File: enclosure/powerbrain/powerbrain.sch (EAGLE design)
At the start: 41 parts, among them J3 AVR_SPI_PRG_6PTH, Q1 FDD4141TO252, Q2 200mA/50V, U2 TPS61090, X2 ZX62D-B-5PA8

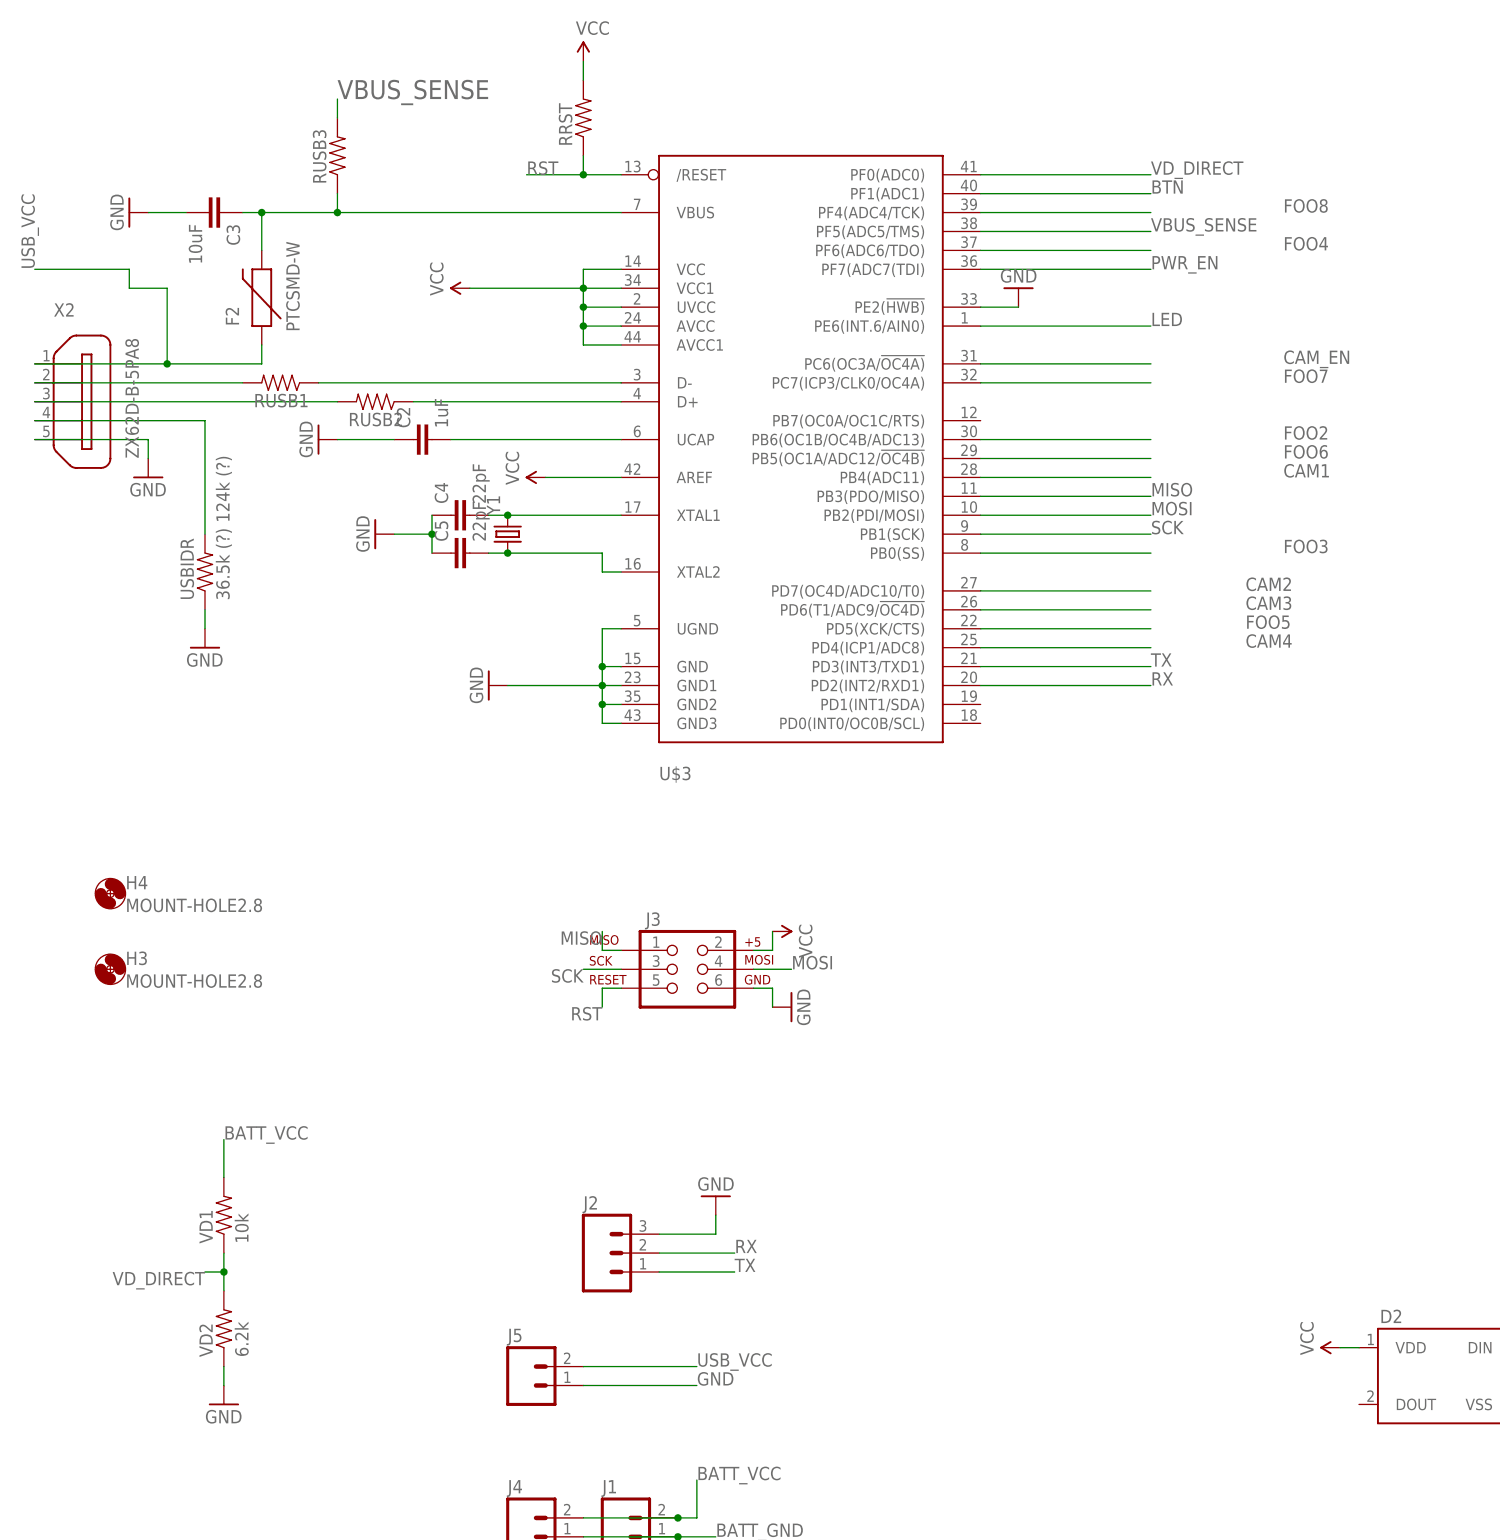
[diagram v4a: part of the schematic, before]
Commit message: powerbrain: VBUS switch
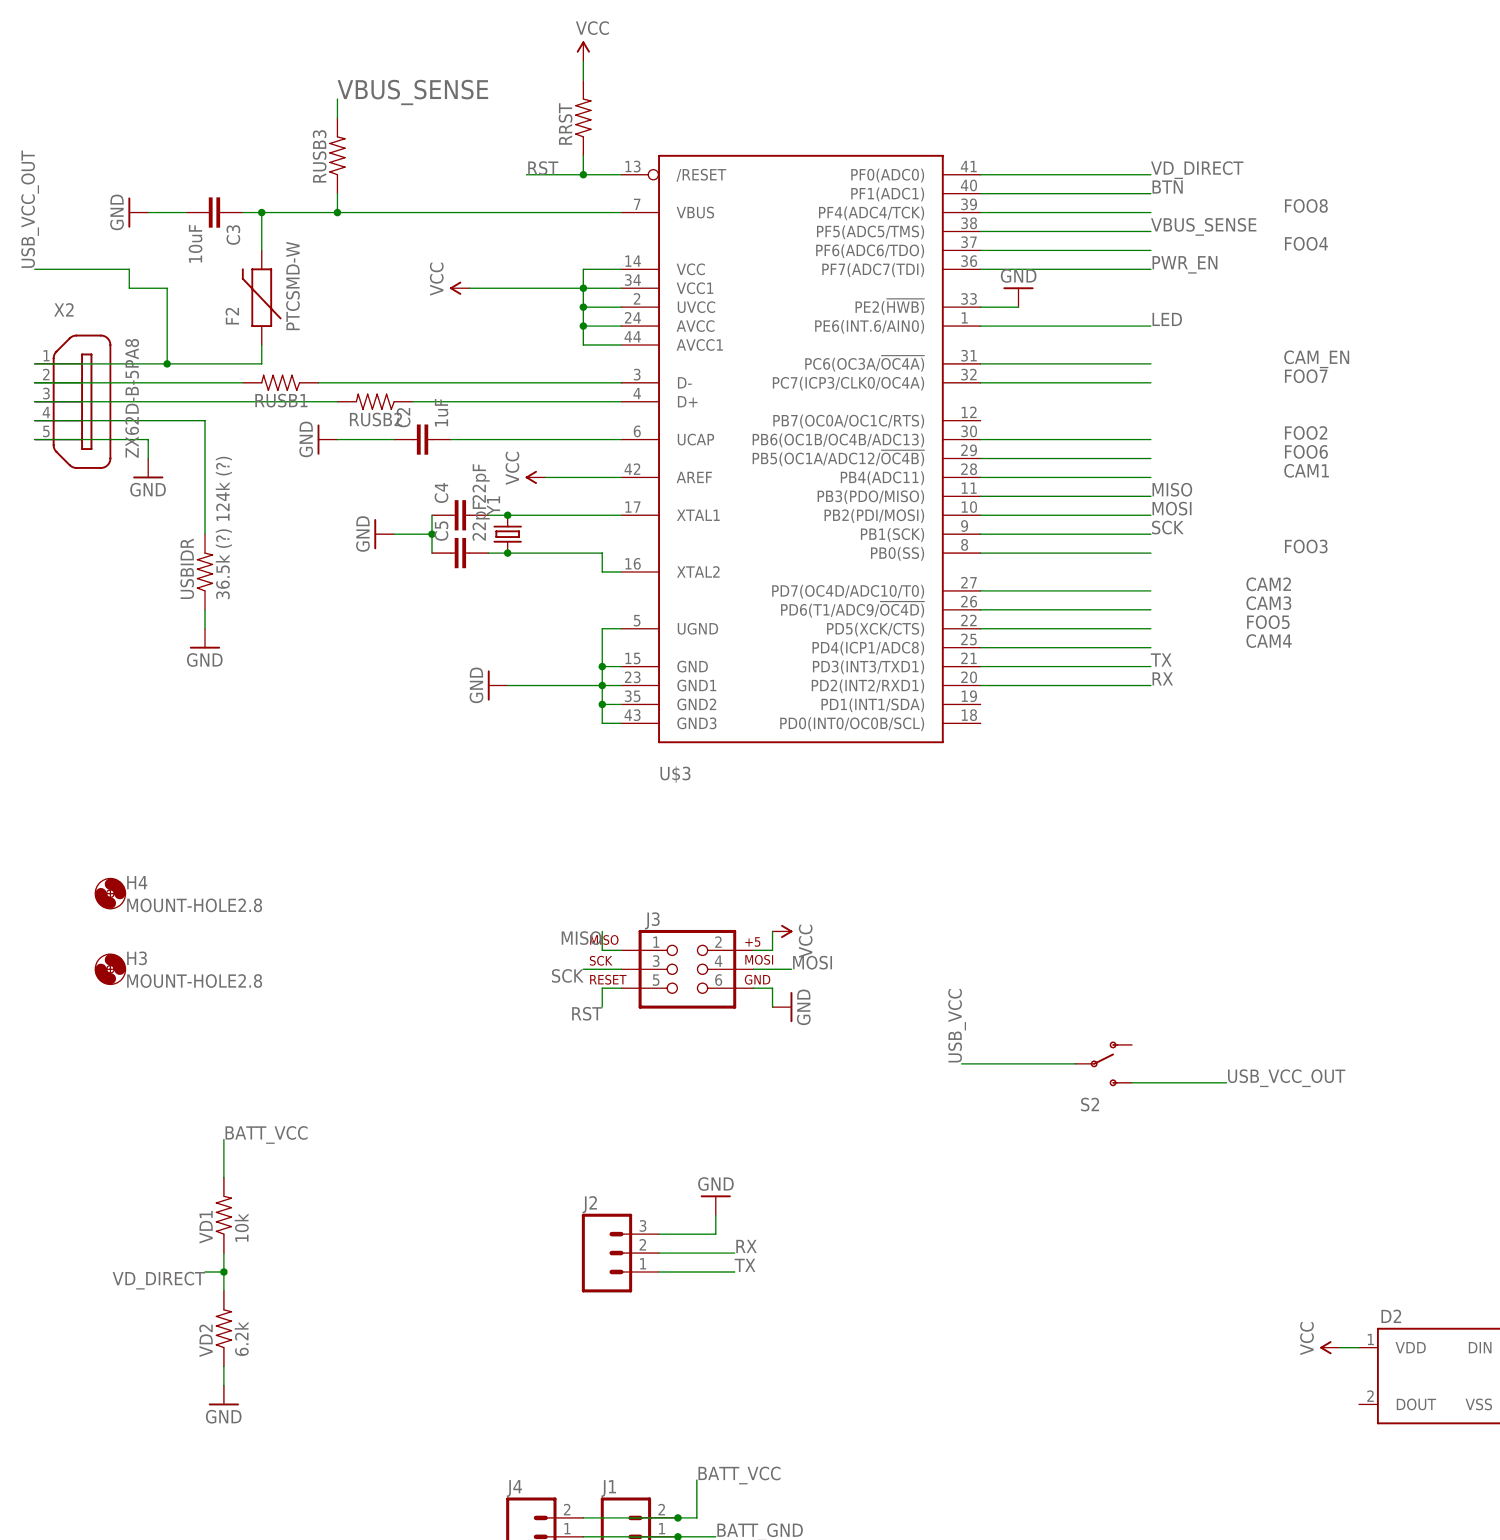
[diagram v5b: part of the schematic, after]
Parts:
- removed J5: (no value), SparkFun-Connectors:M02LOCK
- added S2: (no value), SparkFun-Electromechanical:SWITCH-SPDTSMD2
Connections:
- new net USB_VCC_OUT: F2.1, S2.S, X2G$1.1
- net GND: no longer J5.1
- net USB_VCC: now also S2.P; no longer F2.1, J5.2, X2G$1.1

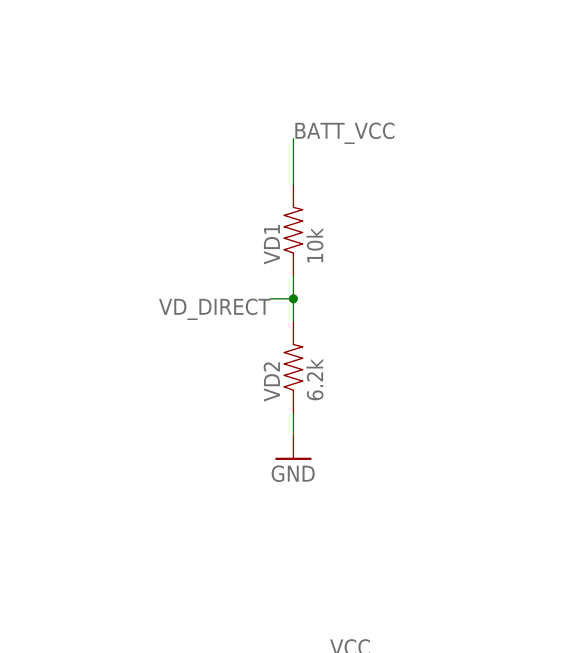
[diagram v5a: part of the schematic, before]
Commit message: powerbrain: decoupling capacitor for battery voltage divider
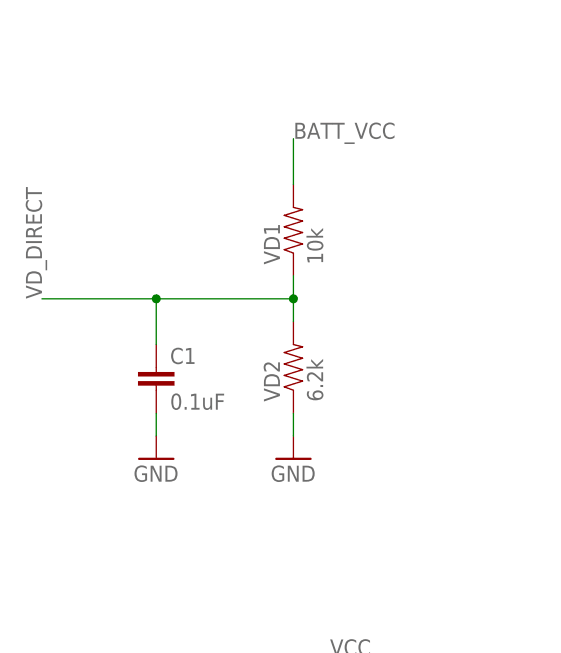
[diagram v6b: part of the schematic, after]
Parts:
- added C1: 0.1uF, SparkFun-Passives:CAP1206
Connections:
- net GND: now also C1.2
- net VD_DIRECT: now also C1.1
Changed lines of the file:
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@@
 <part name="RUSB3" library="SparkFun-Passives" deviceset="RESISTOR" device="1206"/>
 <part name="S2" library="SparkFun-Electromechanical" deviceset="SWITCH-SPDT" device="SMD2"/>
+<part name="C1" library="SparkFun-Passives" deviceset="CAP" device="1206" value="0.1uF"/>
+<part name="GND3" library="SparkFun-Aesthetics" deviceset="GND" device=""/>
 </parts>
 <sheets>
@@
 <instance part="RUSB3" gate="G$1" x="53.34" y="228.6" rot="R90"/>
 <instance part="S2" gate="1" x="154.94" y="106.68"/>
+<instance part="C1" gate="G$1" x="22.86" y="68.58"/>
+<instance part="GND3" gate="1" x="22.86" y="60.96"/>
 </instances>
 <busses>
@@
 <pinref part="J2" gate="J$1" pin="3"/>
 </segment>
+<segment>
+<pinref part="GND3" gate="1" pin="GND"/>
+<pinref part="C1" gate="G$1" pin="2"/>
+<wire x1="22.86" y1="63.5" x2="22.86" y2="66.04" width="0.1524" layer="91"/>
+</segment>
 </net>
 <net name="RX" class="0">
@@
 <wire x1="38.1" y1="81.28" x2="38.1" y2="78.74" width="0.1524" layer="91"/>
 <wire x1="38.1" y1="78.74" x2="38.1" y2="76.2" width="0.1524" layer="91"/>
-<wire x1="38.1" y1="78.74" x2="35.56" y2="78.74" width="0.1524" layer="91"/>
+<wire x1="38.1" y1="78.74" x2="22.86" y2="78.74" width="0.1524" layer="91"/>
 <junction x="38.1" y="78.74"/>
-<label x="35.56" y="78.74" size="1.778" layer="95" rot="R180"/>
-</segment>
-<segment>
+<label x="10.16" y="78.74" size="1.778" layer="95" rot="R90"/>
+<pinref part="C1" gate="G$1" pin="1"/>
+<wire x1="22.86" y1="78.74" x2="10.16" y2="78.74" width="0.1524" layer="91"/>
+<wire x1="22.86" y1="73.66" x2="22.86" y2="78.74" width="0.1524" layer="91"/>
+<junction x="22.86" y="78.74"/>
+</segment>
+<segment>

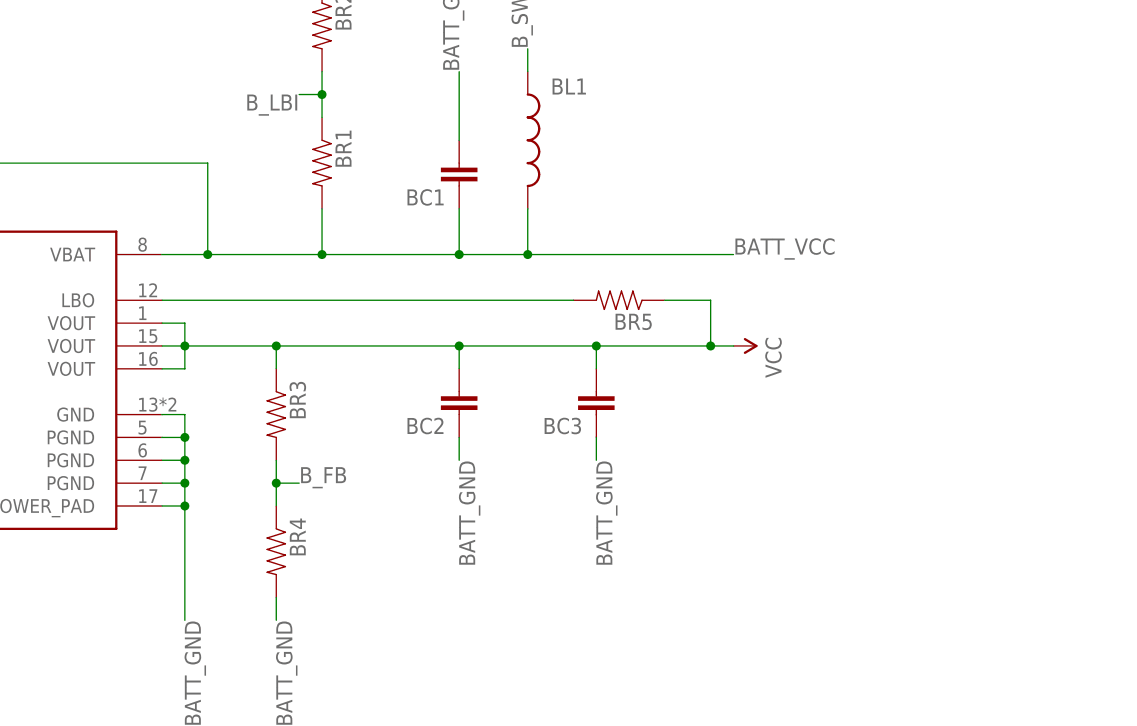
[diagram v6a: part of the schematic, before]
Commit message: powerbrain: low battery output
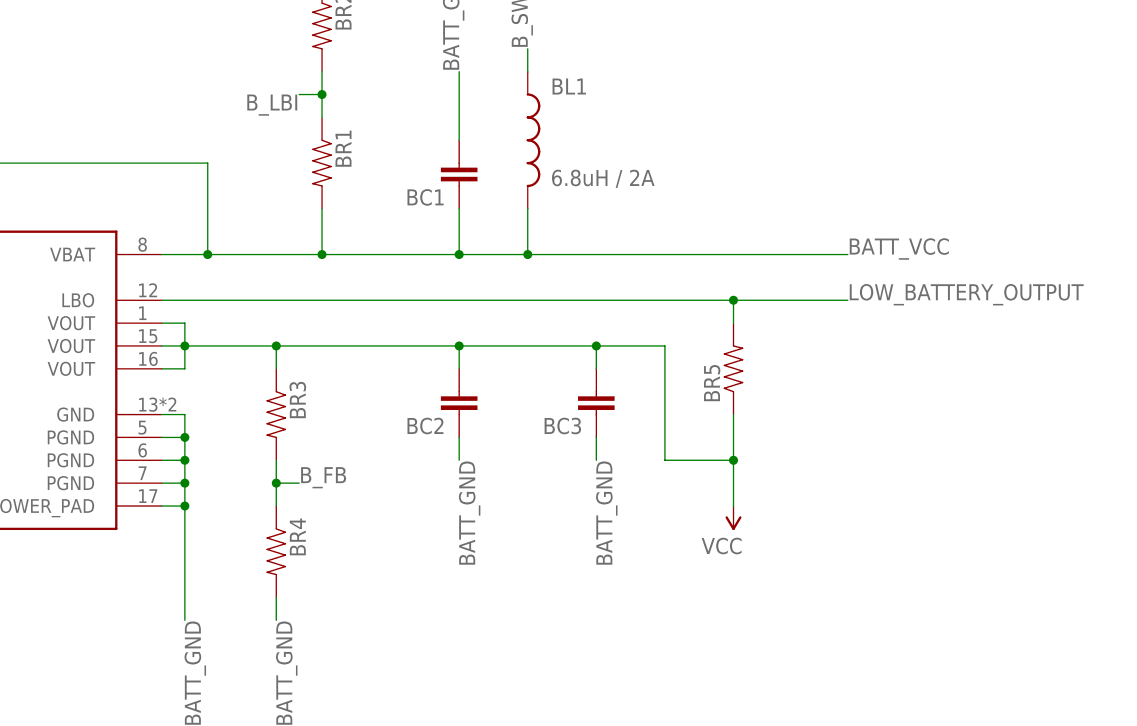
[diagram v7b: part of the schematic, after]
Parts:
- BL1: value (none) -> 6.8uH / 2A
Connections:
- net N$16 renamed LOW_BATTERY_OUTPUT
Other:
- moved on the sheet: BR5
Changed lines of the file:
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@@
 <?xml version="1.0" encoding="utf-8"?>
 <!DOCTYPE eagle SYSTEM "eagle.dtd">
-<eagle version="8.2.1">
+<eagle version="8.2.2">
 <drawing>
 <settings>
@@
 <part name="VD2" library="SparkFun-Passives" deviceset="RESISTOR" device="1206" value="6.2k"/>
 <part name="J1" library="SparkFun-Connectors" deviceset="M02" device="LOCK"/>
-<part name="BL1" library="SparkFun-Passives" deviceset="INDUCTOR" device="NPI75"/>
+<part name="BL1" library="SparkFun-Passives" deviceset="INDUCTOR" device="NPI75" value="6.8uH / 2A"/>
 <part name="GND6" library="SparkFun-Aesthetics" deviceset="GND" device=""/>
 <part name="R3" library="SparkFun-Resistors" deviceset="RESISTOR" device="1206" value="10k"/>
@@
 <instance part="BC2" gate="G$1" x="317.5" y="182.88" rot="R180"/>
 <instance part="BC3" gate="G$1" x="332.74" y="182.88" rot="R180"/>
-<instance part="BR5" gate="G$1" x="335.28" y="193.04" rot="R180"/>
+<instance part="BR5" gate="G$1" x="347.98" y="185.42" rot="R90"/>
 <instance part="BR1" gate="G$1" x="302.26" y="208.28" rot="R270"/>
 <instance part="BR2" gate="G$1" x="302.26" y="223.52" rot="R270"/>
@@
 <instance part="GND4" gate="1" x="104.14" y="88.9" rot="R180"/>
 <instance part="U2" gate="G$1" x="266.7" y="187.96"/>
-<instance part="SUPPLY7" gate="G$1" x="347.98" y="187.96" rot="R270"/>
+<instance part="SUPPLY7" gate="G$1" x="347.98" y="170.18" rot="R180"/>
 <instance part="J2" gate="J$1" x="88.9" y="81.28"/>
 <instance part="J4" gate="G$1" x="78.74" y="43.18"/>
@@
 <wire x1="297.18" y1="187.96" x2="317.5" y2="187.96" width="0.1524" layer="91"/>
 <wire x1="317.5" y1="187.96" x2="332.74" y2="187.96" width="0.1524" layer="91"/>
-<wire x1="332.74" y1="187.96" x2="345.44" y2="187.96" width="0.1524" layer="91"/>
-<wire x1="345.44" y1="187.96" x2="347.98" y2="187.96" width="0.1524" layer="91"/>
+<wire x1="332.74" y1="187.96" x2="340.36" y2="187.96" width="0.1524" layer="91"/>
+<wire x1="340.36" y1="187.96" x2="340.36" y2="175.26" width="0.1524" layer="91"/>
+<wire x1="340.36" y1="175.26" x2="347.98" y2="175.26" width="0.1524" layer="91"/>
+<wire x1="347.98" y1="175.26" x2="347.98" y2="170.18" width="0.1524" layer="91"/>
 <wire x1="297.18" y1="187.96" x2="297.18" y2="185.42" width="0.1524" layer="91"/>
 <junction x="297.18" y="187.96"/>
@@
 <junction x="332.74" y="187.96"/>
 <pinref part="BR5" gate="G$1" pin="1"/>
-<wire x1="340.36" y1="193.04" x2="345.44" y2="193.04" width="0.1524" layer="91"/>
-<wire x1="345.44" y1="193.04" x2="345.44" y2="187.96" width="0.1524" layer="91"/>
-<junction x="345.44" y="187.96"/>
+<wire x1="347.98" y1="180.34" x2="347.98" y2="175.26" width="0.1524" layer="91"/>
+<junction x="347.98" y="175.26"/>
 <pinref part="U2" gate="G$1" pin="VOUT@2"/>
 <pinref part="U2" gate="G$1" pin="VOUT@3"/>
@@
 <junction x="317.5" y="198.12"/>
 <wire x1="317.5" y1="198.12" x2="325.12" y2="198.12" width="0.1524" layer="91"/>
-<wire x1="347.98" y1="198.12" x2="325.12" y2="198.12" width="0.1524" layer="91"/>
+<wire x1="360.68" y1="198.12" x2="325.12" y2="198.12" width="0.1524" layer="91"/>
 <pinref part="BL1" gate="G$1" pin="2"/>
 <wire x1="325.12" y1="203.2" x2="325.12" y2="198.12" width="0.1524" layer="91"/>
 <junction x="325.12" y="198.12"/>
-<label x="347.98" y="198.12" size="1.778" layer="95"/>
+<label x="360.68" y="198.12" size="1.778" layer="95"/>
 <wire x1="289.56" y1="198.12" x2="289.56" y2="208.28" width="0.1524" layer="91"/>
 <junction x="289.56" y="198.12"/>
@@
 </segment>
 </net>
-<net name="N$16" class="0">
+<net name="LOW_BATTERY_OUTPUT" class="0">
 <segment>
 <pinref part="BR5" gate="G$1" pin="2"/>
-<wire x1="330.2" y1="193.04" x2="284.48" y2="193.04" width="0.1524" layer="91"/>
+<wire x1="347.98" y1="190.5" x2="347.98" y2="193.04" width="0.1524" layer="91"/>
+<wire x1="347.98" y1="193.04" x2="284.48" y2="193.04" width="0.1524" layer="91"/>
 <pinref part="U2" gate="G$1" pin="LBO"/>
-</segment>
-</net>
+<wire x1="347.98" y1="193.04" x2="360.68" y2="193.04" width="0.1524" layer="91"/>
+<junction x="347.98" y="193.04"/>
+<label x="360.68" y="193.04" size="1.778" layer="95"/>
+</segment>
+</net>
